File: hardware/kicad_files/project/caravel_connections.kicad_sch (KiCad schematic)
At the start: 13 parts, among them J1 Conn_01x03_Pin, J2 Conn_01x03_Pin, J3 Conn_01x03_Pin, U2 C2977809

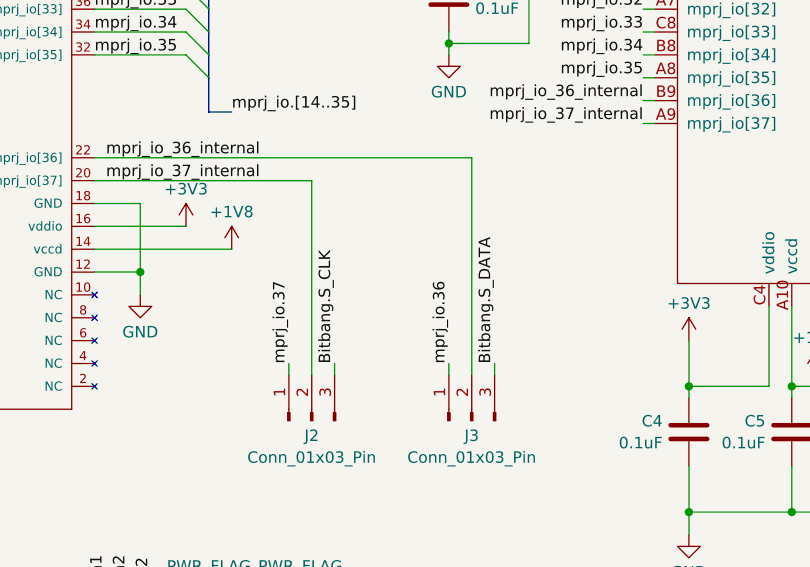
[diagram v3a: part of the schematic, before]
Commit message: fix: rename and reconnect S_DATA and S_CLK
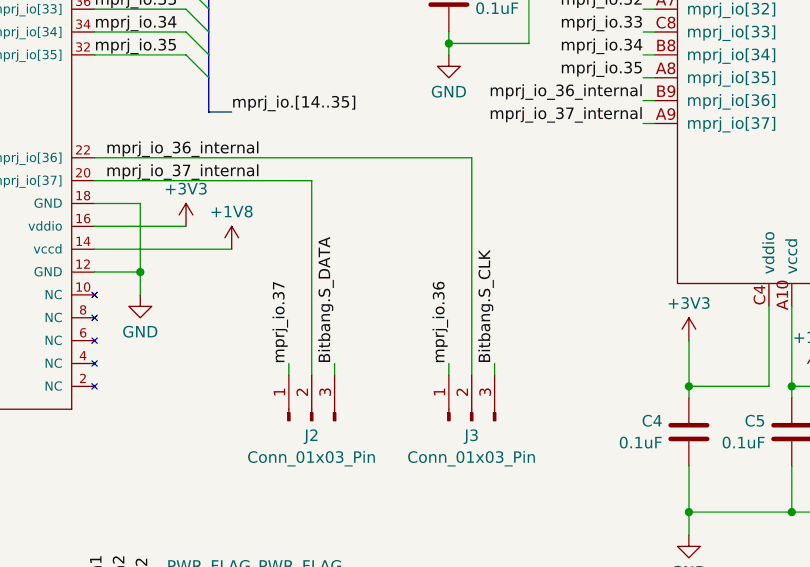
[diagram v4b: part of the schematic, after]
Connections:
- net Bitbang.S_CLK: now also J3.3 (Pin_3); no longer J2.3 (Pin_3)
- net Bitbang.S_DATA: now also J2.3 (Pin_3); no longer J3.3 (Pin_3)
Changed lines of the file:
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@@
 		)
 	)
-	(label "Bitbang.S_DATA"
+	(label "Bitbang.S_CLK"
 		(at 160.02 133.35 90)
 		(fields_autoplaced yes)
@@
 		)
 	)
-	(label "Bitbang.S_CLK"
+	(label "Bitbang.S_DATA"
 		(at 142.24 133.35 90)
 		(fields_autoplaced yes)

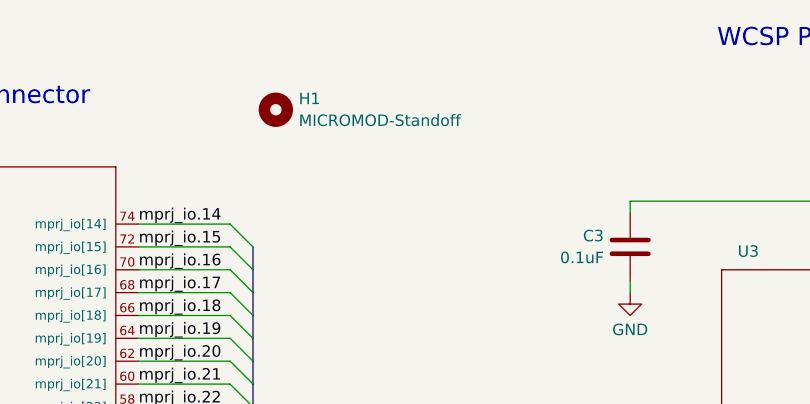
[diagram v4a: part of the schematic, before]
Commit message: fix: replace all local symbols and footprints with versions from KiCad or project libraries
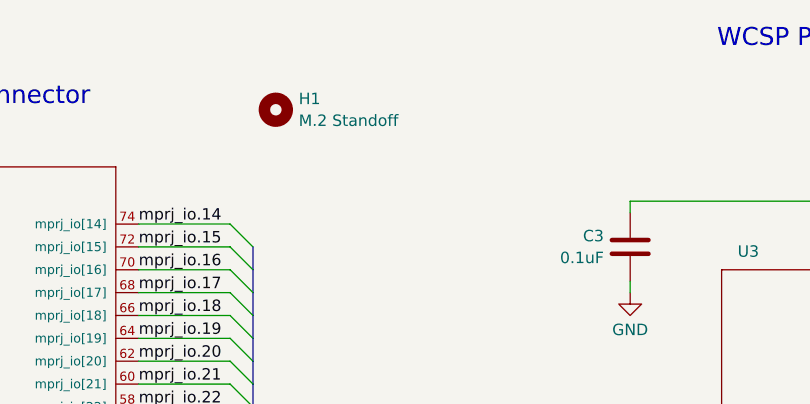
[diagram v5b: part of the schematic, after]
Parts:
- H1: value MICROMOD-Standoff -> M.2 Standoff
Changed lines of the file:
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@@
 		(dnp no)
 		(fields_autoplaced yes)
-		(property "Reference" "#PWR024"
+		(property "Reference" "#PWR030"
 			(at 181.61 158.75 0)
 			(effects
@@
 			(project "FABulous_board"
 				(path "/5664f05e-a3ef-4177-8026-c4580fa32c71/98d779a6-157c-40ed-a845-7459375f17fe"
-					(reference "#PWR024")
+					(reference "#PWR030")
 					(unit 1)
 				)
@@
 		(dnp no)
 		(fields_autoplaced yes)
-		(property "Reference" "#PWR014"
+		(property "Reference" "#PWR020"
 			(at 50.8 118.11 0)
 			(effects
@@
 			(project ""
 				(path "/5664f05e-a3ef-4177-8026-c4580fa32c71/98d779a6-157c-40ed-a845-7459375f17fe"
-					(reference "#PWR014")
+					(reference "#PWR020")
 					(unit 1)
 				)
@@
 		(dnp no)
 		(fields_autoplaced yes)
-		(property "Reference" "#PWR029"
+		(property "Reference" "#PWR035"
 			(at 266.7 106.68 0)
 			(effects
@@
 			(project "FABulous_board"
 				(path "/5664f05e-a3ef-4177-8026-c4580fa32c71/98d779a6-157c-40ed-a845-7459375f17fe"
-					(reference "#PWR029")
+					(reference "#PWR035")
 					(unit 1)
 				)
@@
 		(dnp no)
 		(fields_autoplaced yes)
-		(property "Reference" "#PWR025"
+		(property "Reference" "#PWR031"
 			(at 195.58 138.43 0)
 			(effects
@@
 			(project ""
 				(path "/5664f05e-a3ef-4177-8026-c4580fa32c71/98d779a6-157c-40ed-a845-7459375f17fe"
-					(reference "#PWR025")
+					(reference "#PWR031")
 					(unit 1)
 				)
@@
 		(dnp no)
 		(fields_autoplaced yes)
-		(property "Reference" "#PWR028"
+		(property "Reference" "#PWR034"
 			(at 236.22 57.15 0)
 			(effects
@@
 			(project "FABulous_board"
 				(path "/5664f05e-a3ef-4177-8026-c4580fa32c71/98d779a6-157c-40ed-a845-7459375f17fe"
-					(reference "#PWR028")
+					(reference "#PWR034")
 					(unit 1)
 				)
@@
 		(dnp no)
 		(fields_autoplaced yes)
-		(property "Reference" "#PWR013"
+		(property "Reference" "#PWR019"
 			(at 48.26 106.68 0)
 			(effects
@@
 			(project "FABulous_board"
 				(path "/5664f05e-a3ef-4177-8026-c4580fa32c71/98d779a6-157c-40ed-a845-7459375f17fe"
-					(reference "#PWR013")
+					(reference "#PWR019")
 					(unit 1)
 				)
@@
 			)
 		)
-		(property "Value" "MICROMOD-Standoff"
+		(property "Value" "M.2 Standoff"
 			(at 133.35 34.2321 0)
 			(effects
@@
 		(dnp no)
 		(fields_autoplaced yes)
-		(property "Reference" "#PWR019"
+		(property "Reference" "#PWR025"
 			(at 125.73 121.92 0)
 			(effects
@@
 			(project ""
 				(path "/5664f05e-a3ef-4177-8026-c4580fa32c71/98d779a6-157c-40ed-a845-7459375f17fe"
-					(reference "#PWR019")
+					(reference "#PWR025")
 					(unit 1)
 				)
@@
 		(dnp no)
 		(fields_autoplaced yes)
-		(property "Reference" "#PWR017"
+		(property "Reference" "#PWR023"
 			(at 100.33 151.13 0)
 			(effects
@@
 			(project "FABulous_board"
 				(path "/5664f05e-a3ef-4177-8026-c4580fa32c71/98d779a6-157c-40ed-a845-7459375f17fe"
-					(reference "#PWR017")
+					(reference "#PWR023")
 					(unit 1)
 				)
@@
 		(dnp no)
 		(fields_autoplaced yes)
-		(property "Reference" "#PWR015"
+		(property "Reference" "#PWR021"
 			(at 58.42 132.08 0)
 			(effects
@@
 			(project ""
 				(path "/5664f05e-a3ef-4177-8026-c4580fa32c71/98d779a6-157c-40ed-a845-7459375f17fe"
-					(reference "#PWR015")
+					(reference "#PWR021")
 					(unit 1)
 				)
@@
 		(dnp no)
 		(fields_autoplaced yes)
-		(property "Reference" "#FLG03"
+		(property "Reference" "#FLG04"
 			(at 138.43 158.115 0)
 			(effects
@@
 			(project "FABulous_board"
 				(path "/5664f05e-a3ef-4177-8026-c4580fa32c71/98d779a6-157c-40ed-a845-7459375f17fe"
-					(reference "#FLG03")
+					(reference "#FLG04")
 					(unit 1)
 				)
@@
 		(dnp no)
 		(fields_autoplaced yes)
-		(property "Reference" "#PWR022"
+		(property "Reference" "#PWR028"
 			(at 170.18 59.69 0)
 			(effects
@@
 			(project "FABulous_board"
 				(path "/5664f05e-a3ef-4177-8026-c4580fa32c71/98d779a6-157c-40ed-a845-7459375f17fe"
-					(reference "#PWR022")
+					(reference "#PWR028")
 					(unit 1)
 				)
@@
 		(dnp no)
 		(fields_autoplaced yes)
-		(property "Reference" "#PWR020"
+		(property "Reference" "#PWR026"
 			(at 130.81 124.46 0)
 			(effects
@@
 			(project ""
 				(path "/5664f05e-a3ef-4177-8026-c4580fa32c71/98d779a6-157c-40ed-a845-7459375f17fe"
-					(reference "#PWR020")
+					(reference "#PWR026")
 					(unit 1)
 				)
@@
 		(dnp no)
 		(fields_autoplaced yes)
-		(property "Reference" "#PWR018"
+		(property "Reference" "#PWR024"
 			(at 120.65 132.08 0)
 			(effects
@@
 			(project "FABulous_board"
 				(path "/5664f05e-a3ef-4177-8026-c4580fa32c71/98d779a6-157c-40ed-a845-7459375f17fe"
-					(reference "#PWR018")
+					(reference "#PWR024")
 					(unit 1)
 				)
@@
 		(dnp no)
 		(fields_autoplaced yes)
-		(property "Reference" "#PWR021"
+		(property "Reference" "#PWR027"
 			(at 154.94 105.41 0)
 			(effects
@@
 			(project "FABulous_board"
 				(path "/5664f05e-a3ef-4177-8026-c4580fa32c71/98d779a6-157c-40ed-a845-7459375f17fe"
-					(reference "#PWR021")
+					(reference "#PWR027")
 					(unit 1)
 				)
@@
 		(dnp no)
 		(fields_autoplaced yes)
-		(property "Reference" "#PWR026"
+		(property "Reference" "#PWR032"
 			(at 228.6 36.83 0)
 			(effects
@@
 			(project ""
 				(path "/5664f05e-a3ef-4177-8026-c4580fa32c71/98d779a6-157c-40ed-a845-7459375f17fe"
-					(reference "#PWR026")
+					(reference "#PWR032")
 					(unit 1)
 				)
@@
 		(dnp no)
 		(fields_autoplaced yes)
-		(property "Reference" "#FLG02"
+		(property "Reference" "#FLG03"
 			(at 128.27 158.115 0)
 			(effects
@@
 			(project ""
 				(path "/5664f05e-a3ef-4177-8026-c4580fa32c71/98d779a6-157c-40ed-a845-7459375f17fe"
-					(reference "#FLG02")
+					(reference "#FLG03")
 					(unit 1)
 				)
@@
 		(dnp no)
 		(fields_autoplaced yes)
-		(property "Reference" "#PWR027"
+		(property "Reference" "#PWR033"
 			(at 232.41 138.43 0)
 			(effects
@@
 			(project "FABulous_board"
 				(path "/5664f05e-a3ef-4177-8026-c4580fa32c71/98d779a6-157c-40ed-a845-7459375f17fe"
-					(reference "#PWR027")
+					(reference "#PWR033")
 					(unit 1)
 				)
@@
 		(dnp no)
 		(fields_autoplaced yes)
-		(property "Reference" "#PWR016"
+		(property "Reference" "#PWR022"
 			(at 63.5 95.25 0)
 			(effects
@@
 			(project ""
 				(path "/5664f05e-a3ef-4177-8026-c4580fa32c71/98d779a6-157c-40ed-a845-7459375f17fe"
-					(reference "#PWR016")
+					(reference "#PWR022")
 					(unit 1)
 				)
@@
 		(dnp no)
 		(fields_autoplaced yes)
-		(property "Reference" "#PWR023"
+		(property "Reference" "#PWR029"
 			(at 181.61 134.62 0)
 			(effects
@@
 			(project ""
 				(path "/5664f05e-a3ef-4177-8026-c4580fa32c71/98d779a6-157c-40ed-a845-7459375f17fe"
-					(reference "#PWR023")
+					(reference "#PWR029")
 					(unit 1)
 				)
@@
 		(dnp no)
 		(fields_autoplaced yes)
-		(property "Reference" "#FLG01"
+		(property "Reference" "#FLG02"
 			(at 107.95 159.385 0)
 			(effects
@@
 			(project "FABulous_board"
 				(path "/5664f05e-a3ef-4177-8026-c4580fa32c71/98d779a6-157c-40ed-a845-7459375f17fe"
-					(reference "#FLG01")
-					(unit 1)
-				)
+					(reference "#FLG02")
+					(unit 1)
+				)
